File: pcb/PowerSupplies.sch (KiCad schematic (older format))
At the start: 13 parts, among them U2 LM2937EM-5.0, U3 LM2937EM-5.0

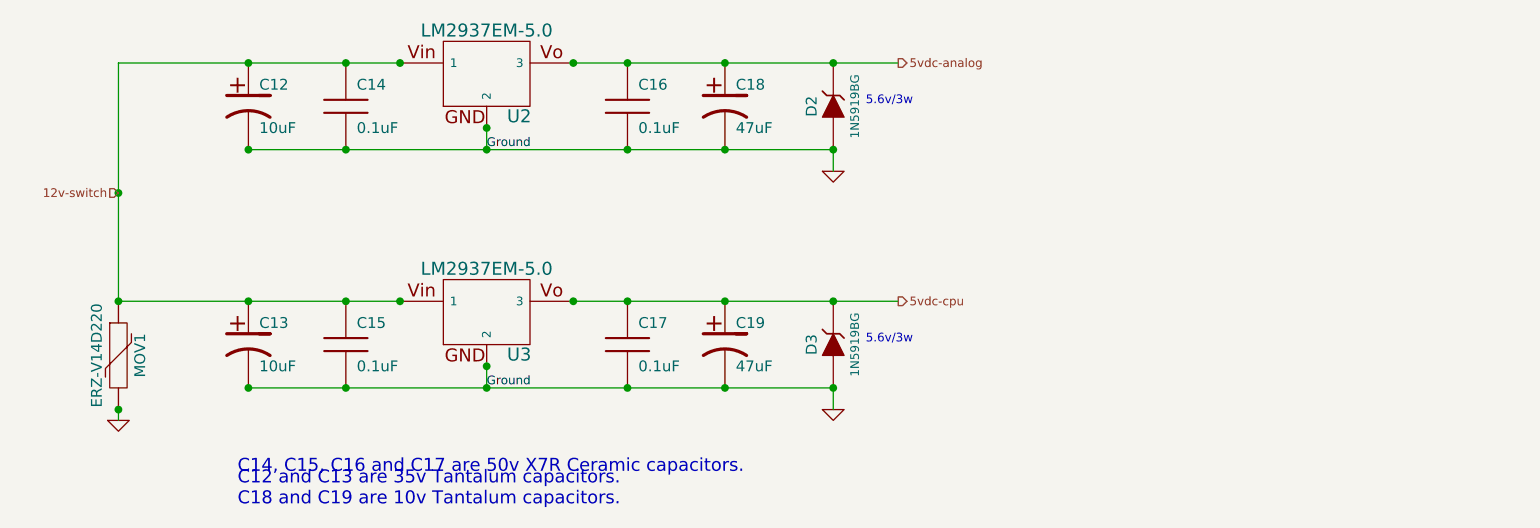
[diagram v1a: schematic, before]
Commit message: Updated schematics, PDFs and PNGs with lumpensack2003 suggestions
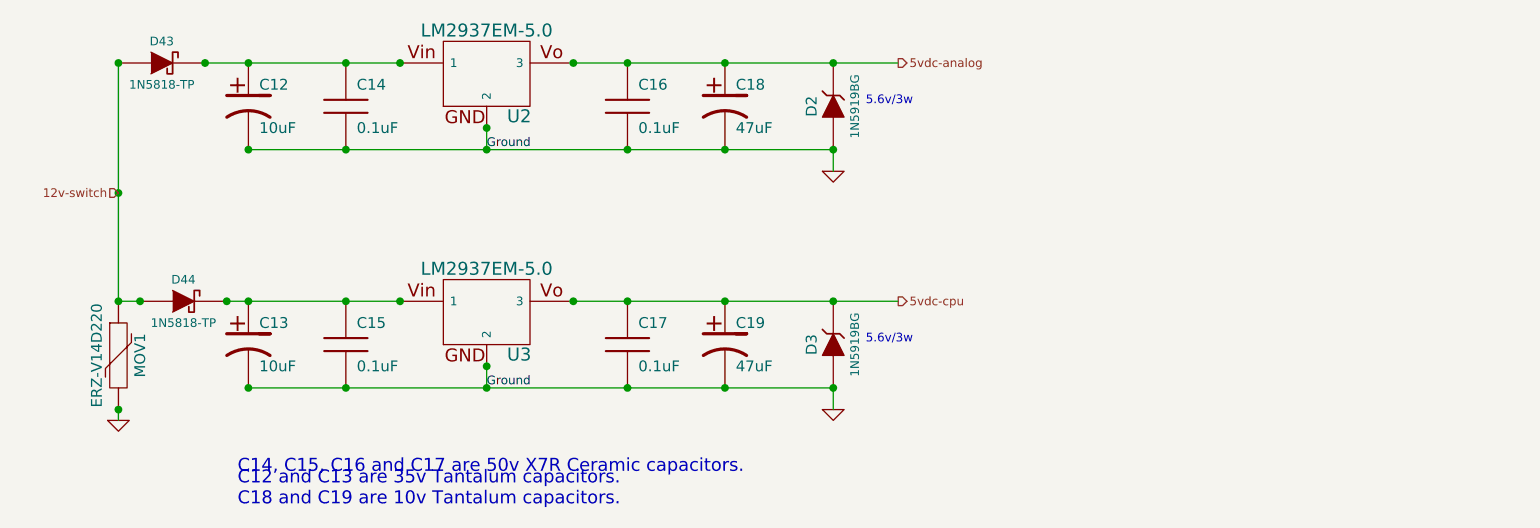
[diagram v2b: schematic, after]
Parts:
- added D43, D44: 1N5818-TP, symbol DIODESCH
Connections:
- net 12v-switch: now also D43.1 (A), D44.1 (A); no longer C12.1, C13.1, C14.1, C15.1, U2.1, U3.1
- new net: C12.1, C14.1, D43.2 (K), U2.1
- new net: C13.1, C15.1, D44.2 (K), U3.1
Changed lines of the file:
@@
-EESchema Schematic File Version 2  date Sun 05 Feb 2012 11:20:52 AM EST
+EESchema Schematic File Version 2  date Sun 05 Feb 2012 10:59:48 PM EST
+LIBS:opto
+LIBS:Jaguar
 LIBS:power
-LIBS:device
-LIBS:transistors
-LIBS:conn
-LIBS:linear
-LIBS:regul
-LIBS:74xx
-LIBS:analog_switches
-LIBS:interface
-LIBS:opto
-LIBS:contrib
-LIBS:Jaguar
 LIBS:Jaguar-cache
 EELAYER 24  0
@@
 Sheet 7 7
 Title "Jaguar PCB for FreeEMS"
-Date "5 feb 2012"
+Date "6 feb 2012"
 Rev "A.2"
 Comp "diyefi.org"
@@
 Comment4 ""
 $EndDescr
-Connection ~ 1750 3350
-Connection ~ 1750 3850
+Connection ~ 1850 3350
+Connection ~ 2250 3350
 Wire Wire Line
-	1750 3850 1750 3900
-Connection ~ 5050 3750
-Connection ~ 5050 3350
-Connection ~ 5050 2650
-Connection ~ 5050 2250
-Connection ~ 3450 2650
+	2250 3350 3050 3350
+Connection ~ 1750 2850
 Wire Wire Line
-	3450 2550 3450 2650
-Connection ~ 4550 3750
-Connection ~ 4550 3350
-Connection ~ 4100 3750
-Connection ~ 4100 3350
-Connection ~ 3850 3350
-Connection ~ 3450 3650
-Connection ~ 2350 3750
-Connection ~ 2800 3750
-Connection ~ 3050 3350
-Connection ~ 2800 3350
-Connection ~ 2350 3350
-Connection ~ 2350 2650
-Connection ~ 2800 2650
-Connection ~ 3450 2550
-Connection ~ 4100 2650
-Connection ~ 4550 2650
-Connection ~ 4550 2250
-Connection ~ 4100 2250
-Connection ~ 3850 2250
-Connection ~ 3050 2250
-Connection ~ 2800 2250
-Connection ~ 2350 2250
+	1750 2250 1750 3350
 Wire Wire Line
-	3850 3350 5350 3350
+	5050 3850 5050 3750
+Wire Wire Line
+	5050 2750 5050 2650
+Wire Wire Line
+	5050 3750 2350 3750
+Connection ~ 3450 3750
+Wire Wire Line
+	3450 3650 3450 3750
+Wire Wire Line
+	5050 2650 2350 2650
 Wire Wire Line
 	3850 2250 5350 2250
 Wire Wire Line
-	3050 2250 1750 2250
+	3850 3350 5350 3350
+Connection ~ 2350 2250
+Connection ~ 2800 2250
+Connection ~ 3050 2250
+Connection ~ 3850 2250
+Connection ~ 4100 2250
+Connection ~ 4550 2250
+Connection ~ 4550 2650
+Connection ~ 4100 2650
+Connection ~ 3450 2550
+Connection ~ 2800 2650
+Connection ~ 2350 2650
+Connection ~ 2350 3350
+Connection ~ 2800 3350
+Connection ~ 3050 3350
+Connection ~ 2800 3750
+Connection ~ 2350 3750
+Connection ~ 3450 3650
+Connection ~ 3850 3350
+Connection ~ 4100 3350
+Connection ~ 4100 3750
+Connection ~ 4550 3350
+Connection ~ 4550 3750
 Wire Wire Line
-	2350 2650 5050 2650
+	3450 2550 3450 2650
+Connection ~ 3450 2650
+Connection ~ 5050 2250
+Connection ~ 5050 2650
+Connection ~ 5050 3350
+Connection ~ 5050 3750
 Wire Wire Line
-	3050 3350 1750 3350
+	1750 3850 1750 3900
+Connection ~ 1750 3850
+Connection ~ 1750 3350
+Connection ~ 1750 2250
 Wire Wire Line
-	3450 3650 3450 3750
-Connection ~ 3450 3750
+	2150 2250 3050 2250
+Connection ~ 2150 2250
 Wire Wire Line
-	2350 3750 5050 3750
-Wire Wire Line
-	5050 2650 5050 2750
-Wire Wire Line
-	5050 3750 5050 3850
-Wire Wire Line
-	1750 3350 1750 2250
-Connection ~ 1750 2850
+	1750 3350 1850 3350
 $Comp
-L GND #PWR060
+L DIODESCH D44
+U 1 1 4F2F40C5
+P 2050 3350
+F 0 "D44" H 2050 3450 40  0000 C CNN
+F 1 "1N5818-TP" H 2050 3250 40  0000 C CNN
+	1    2050 3350
+	1    0    0    -1
+$EndComp
+$Comp
+L DIODESCH D43
+U 1 1 4F2F408F
+P 1950 2250
+F 0 "D43" H 1950 2350 40  0000 C CNN
+F 1 "1N5818-TP" H 1950 2150 40  0000 C CNN
+	1    1950 2250
+	1    0    0    -1
+$EndComp
+$Comp
+L GND #PWR071
 U 1 1 4F24F936
 P 1750 3900
-F 0 "#PWR060" H 1750 3900 30  0001 C CNN
+F 0 "#PWR071" H 1750 3900 30  0001 C CNN
 F 1 "GND" H 1750 3830 30  0001 C CNN
 	1    1750 3900
@@
 12v-switch
 $Comp
-L GND #PWR061
+L GND #PWR072
 U 1 1 4F1C2CDE
 P 5050 3850
-F 0 "#PWR061" H 5050 3850 30  0001 C CNN
+F 0 "#PWR072" H 5050 3850 30  0001 C CNN
 F 1 "GND" H 5050 3780 30  0001 C CNN
 	1    5050 3850
@@
 $EndComp
 $Comp
-L GND #PWR062
+L GND #PWR073
 U 1 1 4F1C2CC1
 P 5050 2750
-F 0 "#PWR062" H 5050 2750 30  0001 C CNN
+F 0 "#PWR073" H 5050 2750 30  0001 C CNN
 F 1 "GND" H 5050 2680 30  0001 C CNN
 	1    5050 2750

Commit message: first commit of Revision A.3 schematic files
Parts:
- added JP10, JP9: JUMPER, symbol JUMPER
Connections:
- net 5vdc-analog: now also JP9.2; no longer C16.1, C18.1, D2.2 (K), U2.3
- net 5vdc-cpu: now also JP10.2; no longer C17.1, C19.1, D3.2 (K), U3.3
- new net: C16.1, C18.1, D2.2 (K), JP9.1, U2.3
- new net: C17.1, C19.1, D3.2 (K), JP10.1, U3.3
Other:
- note added: "JP9 and JP10 allow you to build the power supply\ncircuits and test them before connecting them\nto the rest of the board."
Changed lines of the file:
@@
-EESchema Schematic File Version 2  date Sun 05 Feb 2012 10:59:48 PM EST
+EESchema Schematic File Version 2  date Sat 18 Feb 2012 05:28:44 PM EST
 LIBS:opto
 LIBS:Jaguar
 LIBS:power
+LIBS:conn
 LIBS:Jaguar-cache
 EELAYER 24  0
@@
 Sheet 7 7
 Title "Jaguar PCB for FreeEMS"
-Date "6 feb 2012"
-Rev "A.2"
+Date "18 feb 2012"
+Rev "A3"
 Comp "diyefi.org"
 Comment1 ""
@@
 Comment4 ""
 $EndDescr
+Text Notes 5450 2700 0    60   ~ 0
+JP9 and JP10 allow you to build the power supply\ncircuits and test them before connecting them\nto the rest of the board.
+Connection ~ 5300 3350
+Connection ~ 5900 3350
+Wire Wire Line
+	5900 3350 5950 3350
+Wire Wire Line
+	5300 2250 3850 2250
 Connection ~ 1850 3350
 Connection ~ 2250 3350
@@
 Wire Wire Line
 	5050 2650 2350 2650
-Wire Wire Line
-	3850 2250 5350 2250
-Wire Wire Line
-	3850 3350 5350 3350
 Connection ~ 2350 2250
 Connection ~ 2800 2250
@@
 Wire Wire Line
 	1750 3350 1850 3350
+Wire Wire Line
+	5900 2250 5950 2250
+Connection ~ 5300 2250
+Connection ~ 5900 2250
+Wire Wire Line
+	5300 3350 3850 3350
+$Comp
+L JUMPER JP10
+U 1 1 4F401512
+P 5600 3350
+F 0 "JP10" H 5600 3500 60  0000 C CNN
+F 1 "JUMPER" H 5600 3270 40  0000 C CNN
+	1    5600 3350
+	1    0    0    -1
+$EndComp
+$Comp
+L JUMPER JP9
+U 1 1 4F4014CF
+P 5600 2250
+F 0 "JP9" H 5600 2400 60  0000 C CNN
+F 1 "JUMPER" H 5600 2170 40  0000 C CNN
+	1    5600 2250
+	1    0    0    -1
+$EndComp
 $Comp
 L DIODESCH D44
@@
 $EndComp
 $Comp
-L GND #PWR071
+L GND #PWR040
 U 1 1 4F24F936
 P 1750 3900
-F 0 "#PWR071" H 1750 3900 30  0001 C CNN
+F 0 "#PWR040" H 1750 3900 30  0001 C CNN
 F 1 "GND" H 1750 3830 30  0001 C CNN
 	1    1750 3900
@@
 12v-switch
 $Comp
-L GND #PWR072
+L GND #PWR041
 U 1 1 4F1C2CDE
 P 5050 3850
-F 0 "#PWR072" H 5050 3850 30  0001 C CNN
+F 0 "#PWR041" H 5050 3850 30  0001 C CNN
 F 1 "GND" H 5050 3780 30  0001 C CNN
 	1    5050 3850
@@
 $EndComp
 $Comp
-L GND #PWR073
+L GND #PWR042
 U 1 1 4F1C2CC1
 P 5050 2750
-F 0 "#PWR073" H 5050 2750 30  0001 C CNN
+F 0 "#PWR042" H 5050 2750 30  0001 C CNN
 F 1 "GND" H 5050 2680 30  0001 C CNN
 	1    5050 2750
@@
 	1    0    0    -1
 $EndComp
-Text HLabel 5350 2250 2    40   Output ~ 0
+Text HLabel 5950 2250 2    40   Output ~ 0
 5vdc-analog
-Text HLabel 5350 3350 2    40   Output ~ 0
+Text HLabel 5950 3350 2    40   Output ~ 0
 5vdc-cpu
 $Comp

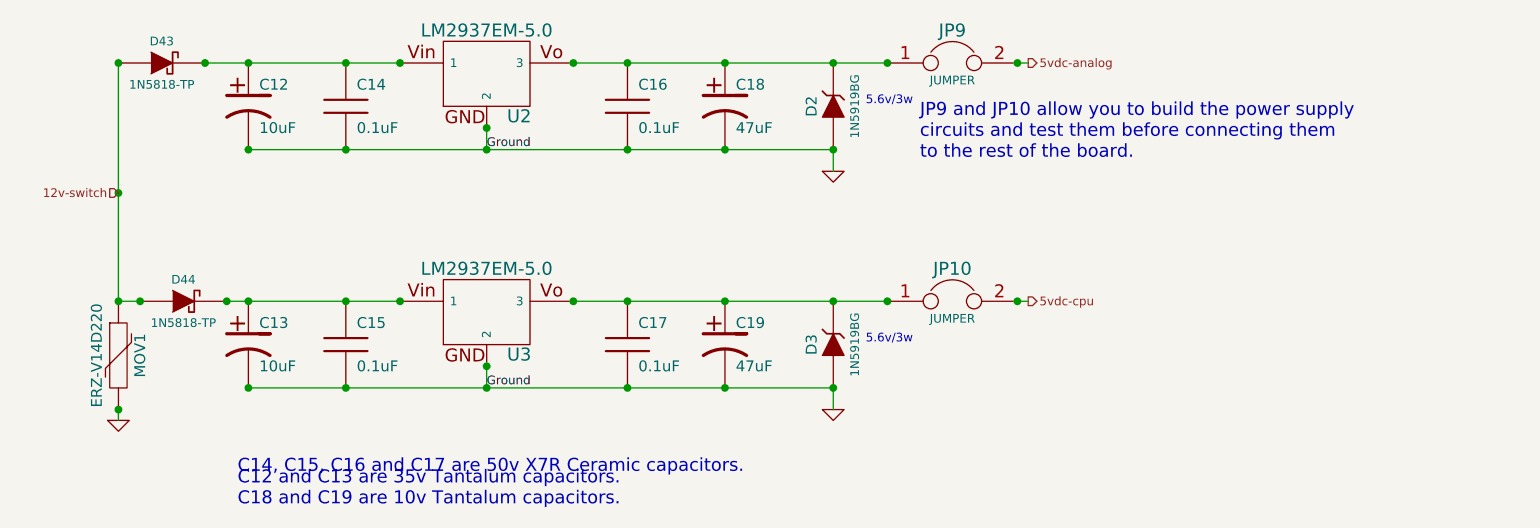
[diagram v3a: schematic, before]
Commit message: Updated schematics for HCPL-061a Optocoupler
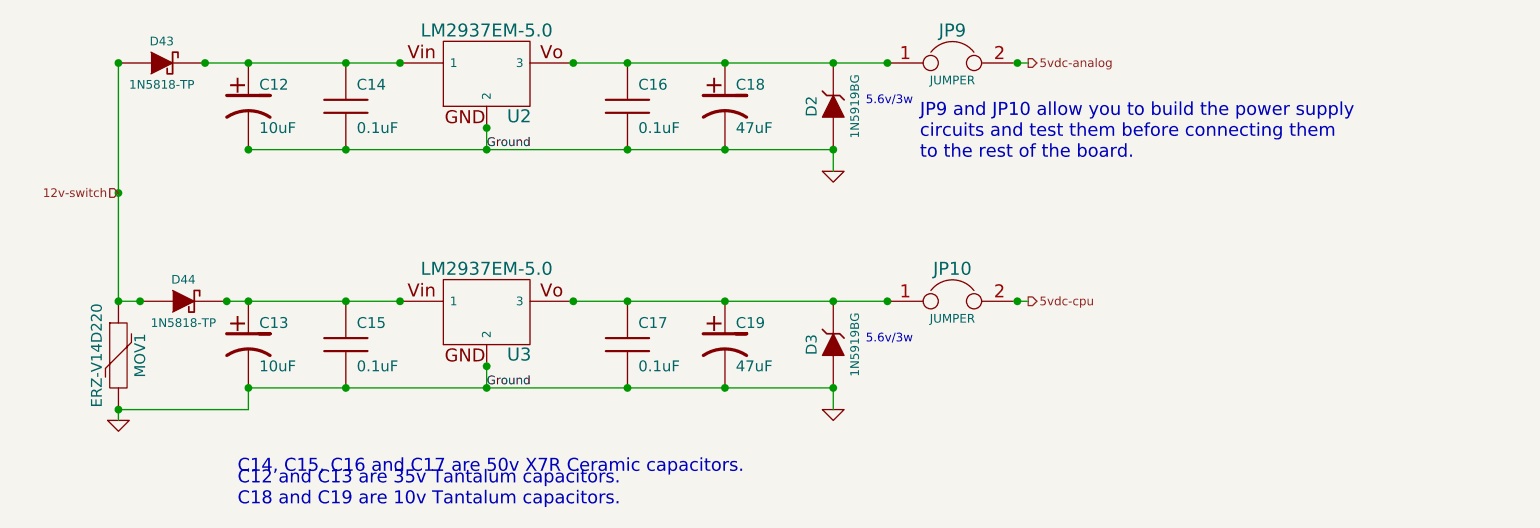
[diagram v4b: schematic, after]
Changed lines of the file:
@@
-EESchema Schematic File Version 2  date Sat 18 Feb 2012 05:28:44 PM EST
+EESchema Schematic File Version 2  date Sun 19 Feb 2012 11:18:36 PM EST
 LIBS:opto
 LIBS:Jaguar
@@
 Sheet 7 7
 Title "Jaguar PCB for FreeEMS"
-Date "18 feb 2012"
+Date "20 feb 2012"
 Rev "A3"
 Comp "diyefi.org"
@@
 Comment4 ""
 $EndDescr
+Wire Wire Line
+	2350 3850 1750 3850
+Wire Wire Line
+	2350 3850 2350 3750
+Wire Wire Line
+	5300 3350 3850 3350
+Connection ~ 5900 2250
+Connection ~ 5300 2250
+Wire Wire Line
+	5900 2250 5950 2250
+Wire Wire Line
+	1850 3350 1750 3350
+Connection ~ 2150 2250
+Wire Wire Line
+	2150 2250 3050 2250
+Connection ~ 1750 2250
+Connection ~ 1750 3350
+Connection ~ 1750 3850
+Wire Wire Line
+	1750 3850 1750 3900
+Connection ~ 5050 3750
+Connection ~ 5050 3350
+Connection ~ 5050 2650
+Connection ~ 5050 2250
+Connection ~ 3450 2650
+Wire Wire Line
+	3450 2550 3450 2650
+Connection ~ 4550 3750
+Connection ~ 4550 3350
+Connection ~ 4100 3750
+Connection ~ 4100 3350
+Connection ~ 3850 3350
+Connection ~ 3450 3650
+Connection ~ 2350 3750
+Connection ~ 2800 3750
+Connection ~ 3050 3350
+Connection ~ 2800 3350
+Connection ~ 2350 3350
+Connection ~ 2350 2650
+Connection ~ 2800 2650
+Connection ~ 3450 2550
+Connection ~ 4100 2650
+Connection ~ 4550 2650
+Connection ~ 4550 2250
+Connection ~ 4100 2250
+Connection ~ 3850 2250
+Connection ~ 3050 2250
+Connection ~ 2800 2250
+Connection ~ 2350 2250
+Wire Wire Line
+	2350 2650 5050 2650
+Wire Wire Line
+	3450 3650 3450 3750
+Connection ~ 3450 3750
+Wire Wire Line
+	2350 3750 5050 3750
+Wire Wire Line
+	5050 2650 5050 2750
+Wire Wire Line
+	5050 3750 5050 3850
+Wire Wire Line
+	1750 3350 1750 2250
+Connection ~ 1750 2850
+Wire Wire Line
+	2250 3350 3050 3350
+Connection ~ 2250 3350
+Connection ~ 1850 3350
+Wire Wire Line
+	5300 2250 3850 2250
+Wire Wire Line
+	5900 3350 5950 3350
+Connection ~ 5900 3350
+Connection ~ 5300 3350
 Text Notes 5450 2700 0    60   ~ 0
 JP9 and JP10 allow you to build the power supply\ncircuits and test them before connecting them\nto the rest of the board.
-Connection ~ 5300 3350
-Connection ~ 5900 3350
-Wire Wire Line
-	5900 3350 5950 3350
-Wire Wire Line
-	5300 2250 3850 2250
-Connection ~ 1850 3350
-Connection ~ 2250 3350
-Wire Wire Line
-	2250 3350 3050 3350
-Connection ~ 1750 2850
-Wire Wire Line
-	1750 2250 1750 3350
-Wire Wire Line
-	5050 3850 5050 3750
-Wire Wire Line
-	5050 2750 5050 2650
-Wire Wire Line
-	5050 3750 2350 3750
-Connection ~ 3450 3750
-Wire Wire Line
-	3450 3650 3450 3750
-Wire Wire Line
-	5050 2650 2350 2650
-Connection ~ 2350 2250
-Connection ~ 2800 2250
-Connection ~ 3050 2250
-Connection ~ 3850 2250
-Connection ~ 4100 2250
-Connection ~ 4550 2250
-Connection ~ 4550 2650
-Connection ~ 4100 2650
-Connection ~ 3450 2550
-Connection ~ 2800 2650
-Connection ~ 2350 2650
-Connection ~ 2350 3350
-Connection ~ 2800 3350
-Connection ~ 3050 3350
-Connection ~ 2800 3750
-Connection ~ 2350 3750
-Connection ~ 3450 3650
-Connection ~ 3850 3350
-Connection ~ 4100 3350
-Connection ~ 4100 3750
-Connection ~ 4550 3350
-Connection ~ 4550 3750
-Wire Wire Line
-	3450 2550 3450 2650
-Connection ~ 3450 2650
-Connection ~ 5050 2250
-Connection ~ 5050 2650
-Connection ~ 5050 3350
-Connection ~ 5050 3750
-Wire Wire Line
-	1750 3850 1750 3900
-Connection ~ 1750 3850
-Connection ~ 1750 3350
-Connection ~ 1750 2250
-Wire Wire Line
-	2150 2250 3050 2250
-Connection ~ 2150 2250
-Wire Wire Line
-	1750 3350 1850 3350
-Wire Wire Line
-	5900 2250 5950 2250
-Connection ~ 5300 2250
-Connection ~ 5900 2250
-Wire Wire Line
-	5300 3350 3850 3350
 $Comp
 L JUMPER JP10

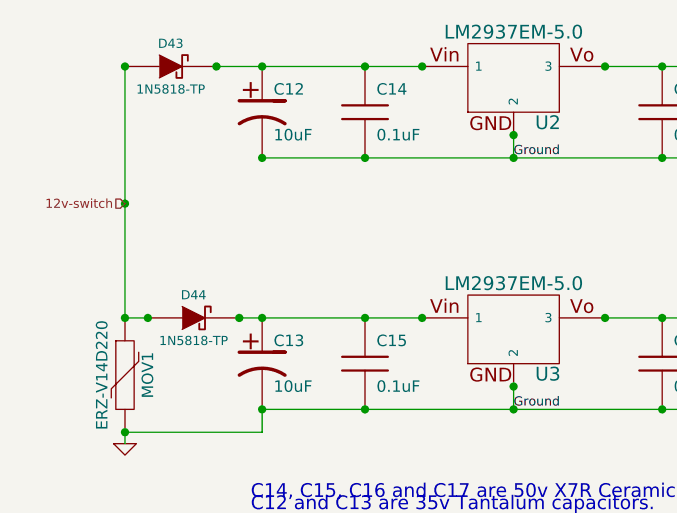
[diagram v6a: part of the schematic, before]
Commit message: Updated TODO.md with changes needed from revision A3 board
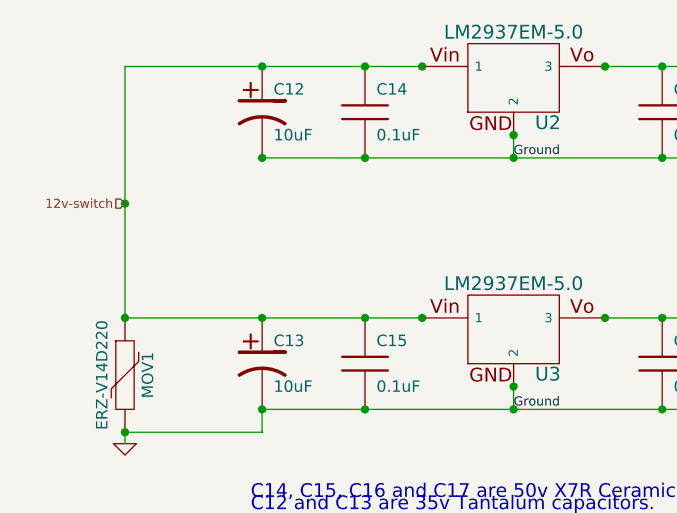
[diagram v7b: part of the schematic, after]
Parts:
- removed D43, D44: 1N5818-TP, symbol DIODESCH
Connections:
- net 12v-switch: now also C12.1, C13.1, C14.1, C15.1, U2.1, U3.1
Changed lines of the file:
@@
-EESchema Schematic File Version 2  date Wed 07 Mar 2012 12:24:35 AM EST
+EESchema Schematic File Version 2  date Sun 15 Apr 2012 10:34:10 AM EDT
 LIBS:opto
 LIBS:Jaguar
@@
 Sheet 7 7
 Title "Jaguar PCB for FreeEMS"
-Date "7 mar 2012"
+Date "15 apr 2012"
 Rev "A3"
 Comp "diyefi.org"
@@
 Comment4 ""
 $EndDescr
+Wire Wire Line
+	3050 3350 1750 3350
 Wire Wire Line
 	2350 3850 1750 3850
@@
 Wire Wire Line
 	5900 2250 5950 2250
-Wire Wire Line
-	1850 3350 1750 3350
-Connection ~ 2150 2250
-Wire Wire Line
-	2150 2250 3050 2250
-Connection ~ 1750 2250
 Connection ~ 1750 3350
 Connection ~ 1750 3850
@@
 Connection ~ 1750 2850
 Wire Wire Line
-	2250 3350 3050 3350
-Connection ~ 2250 3350
-Connection ~ 1850 3350
-Wire Wire Line
 	5300 2250 3850 2250
 Wire Wire Line
@@
 Connection ~ 5900 3350
 Connection ~ 5300 3350
+Wire Wire Line
+	1750 2250 3050 2250
 Text Notes 5450 2700 0    60   ~ 0
 JP9 and JP10 allow you to build the power supply\ncircuits and test them before connecting them\nto the rest of the board.
@@
 	1    0    0    -1
 $EndComp
-$Comp
-L DIODESCH D44
-U 1 1 4F2F40C5
-P 2050 3350
-F 0 "D44" H 2050 3450 40  0000 C CNN
-F 1 "1N5818-TP" H 2050 3250 40  0000 C CNN
-	1    2050 3350
-	1    0    0    -1
-$EndComp
-$Comp
-L DIODESCH D43
-U 1 1 4F2F408F
-P 1950 2250
-F 0 "D43" H 1950 2350 40  0000 C CNN
-F 1 "1N5818-TP" H 1950 2150 40  0000 C CNN
-	1    1950 2250
-	1    0    0    -1
-$EndComp
